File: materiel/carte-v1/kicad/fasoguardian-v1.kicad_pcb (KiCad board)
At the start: 4 copper layers, 41 x 36 mm, 155 parts, among them J3 Antenne LTE, J4 Antenne GNSS active, J5 Nano-SIM, J6 ECT 818011998, J7 SWD Tag-Connect, Q1 2N7002DW, Q2 AO3401A, Q3 2N7002DW, Q4 2N7002DW, Q5 AO3400A, SW1 SOS, U1 STM32U575CIT6, U10 SN74AXC4T774, U11 SN74AXC4T774, U12 ESDA6V1W5, U2 A7670E (variante GNSS), U3 LIS2DW12TR, U4 BQ25180YBGR, U5 TPS63900DSKR, U6 TPS22965DSGR, U7 MAX17048G+T10, U8 ATECC608B-MAHDA, U9 W25Q64JVZPIQ, Y1 32,768 kHz

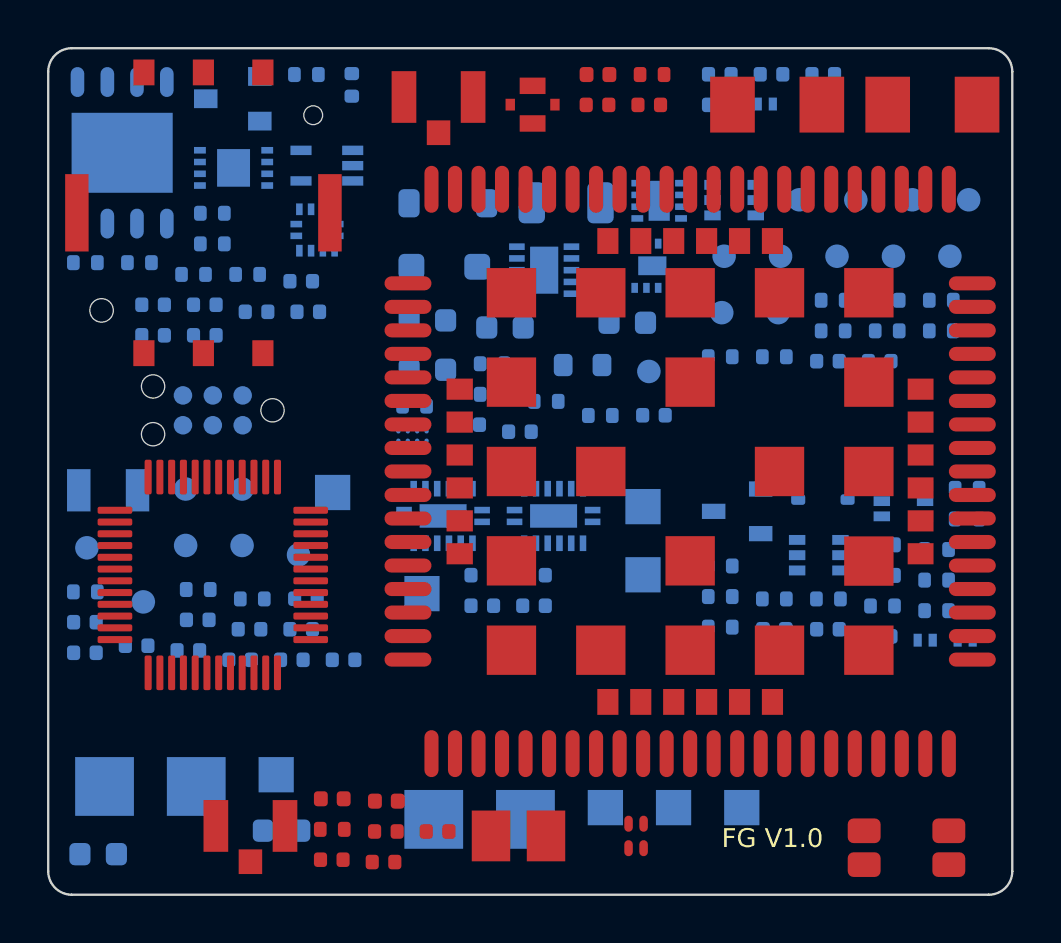
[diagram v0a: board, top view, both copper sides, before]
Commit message: feat(materiel): lignes RF tracées, plans d'alimentation reliés avant routage, routage automatique à 88 %
- lignes LTE et GNSS droites, sans via, de 12,6 et 11,1 mm, réseau d'adaptation aligné, vias de couture
- couche 3 en trois plans (modem, VSYS, 3,3 V), vias de plan posés et verrouillés avant le routage
- Freerouting 2.5 avec éventail ; aucune erreur DRC, parité schéma-carte exacte, 48 liaisons restantes
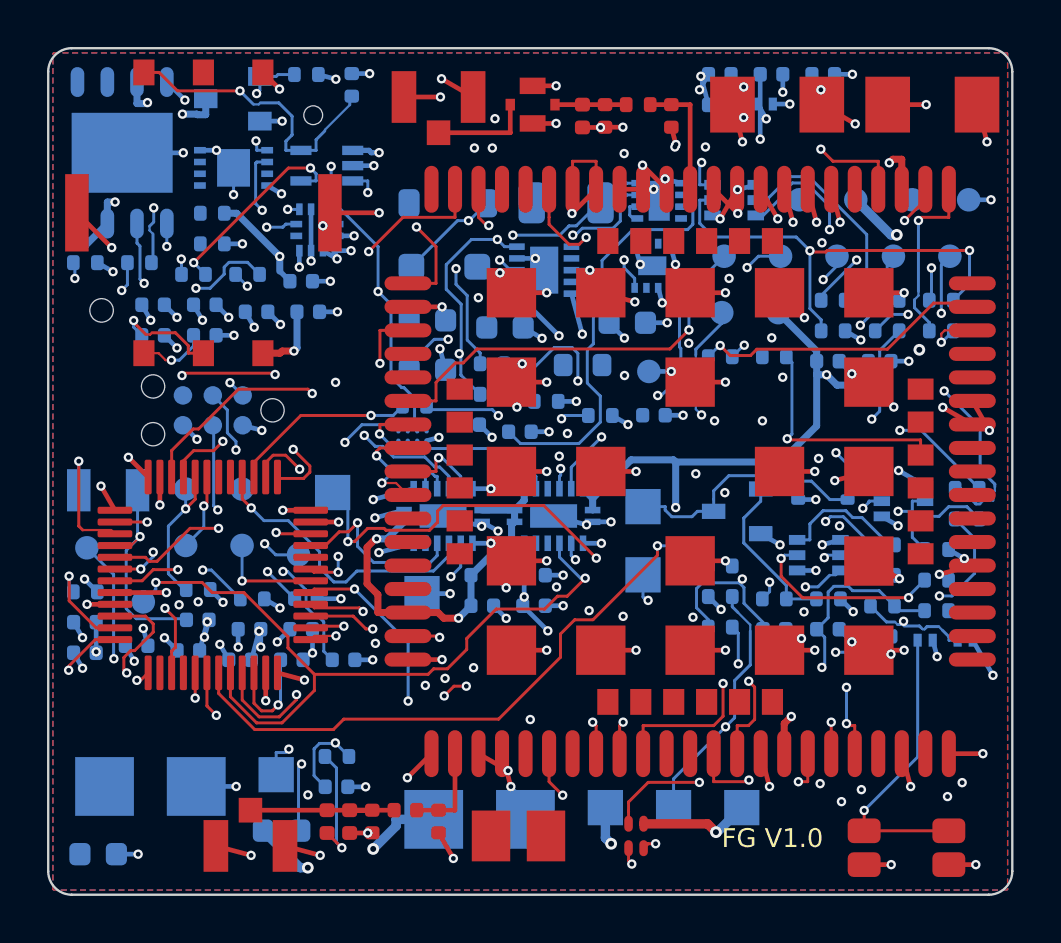
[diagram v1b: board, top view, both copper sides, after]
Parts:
- C25, R23: moved to B.Cu
- moved C25 3.77 mm to (112.3, 131.4)
- moved R23 3.11 mm to (112.3, 130.1)
- moved L2 2.67 mm to (111.9, 132.9), turned to -90 degrees
- moved C23 2.37 mm to (113.8, 132.9), turned to -90 degrees
- moved C22 2.28 mm to (116.6, 132.9), turned to -90 degrees
- moved D4 1.88 mm to (122.7, 102.9), turned to -90 degrees
- moved C24 1.64 mm to (115.2, 132.4), turned to 180 degrees
- moved R20 1.41 mm to (125.1, 102.4), turned to 180 degrees
- moved D5 1.22 mm to (112.8, 132.9), turned to -90 degrees
- moved C20 1.05 mm to (126.5, 102.9), turned to -90 degrees
- moved J4 0.67 mm to (108.6, 133.2), turned to 180 degrees
- moved C21 0.57 mm to (123.7, 102.9), turned to -90 degrees
- turned J6 to 180 degrees
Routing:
- net GND: track 0.00 -> 169.8 mm, vias 0 -> 150
- net I2C_SDA: track 0.00 -> 68.3 mm, vias 0 -> 7
- net 1V8: track 0.00 -> 65.0 mm, vias 0 -> 5
- net SIM_VDD: track 0.00 -> 55.2 mm, vias 0 -> 4
- net SIM_CLK_M: track 0.00 -> 53.2 mm, vias 0 -> 3
- net MCU_PWRKEY: track 0.00 -> 49.5 mm, vias 0 -> 2
- net SIM_RST_M: track 0.00 -> 49.1 mm, vias 0 -> 6
- net LED_R: track 0.00 -> 47.4 mm, vias 0 -> 3
- net GAUGE_ALRT: track 0.00 -> 46.7 mm, vias 0 -> 4
- net MCU_RESET: track 0.00 -> 45.4 mm, vias 0 -> 5
- net MODEM_EN: track 0.00 -> 44.8 mm, vias 0 -> 5
- net SIM_DATA_M: track 0.00 -> 44.2 mm, vias 0 -> 4
- net LOOP: track 0.00 -> 43.4 mm, vias 0 -> 4
- net SOS: track 0.00 -> 41.6 mm, vias 0 -> 3
- net LED_B: track 0.00 -> 40.6 mm, vias 0 -> 3
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- added copper zone on B.Cu, net GND
- added copper zone on F.Cu, net GND
- added copper zone on In2.Cu, net VSYS

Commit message: feat(materiel): carte V1 routée en 6 couches, prête à commander
Routage complet du bracelet sur 41 × 36 mm en 6 couches : aucune liaison
manquante, DRC sans erreur ni avertissement, parité avec le schéma, ERC sans
violation.

- Masse de la couche 2 pleine et interdite aux pistes (référence des lignes
  RF de 50 Ω et de l'USB du modem) ; couche 5 mixte, plans du modem et de la
  batterie interdits aux pistes (ADR 0042, point 9).
- Vias de 0,3/0,15 mm et vias de plan dans les pastilles, bouchés et
  recouverts (capacités JLCPCB en 6 couches).
- Chemin des pointes de 2 A du modem pré-routé et verrouillé, bande de plan
  VBAT dédiée : 25 mΩ de cuivre de la batterie au module au lieu de 140 mΩ
  (ADR 0042, point 10). controler_carte.py le mesure avec resistance.py
  (pistes, vias et plans maillés).
- finir.py : finition par recherche A*, arrachage, négociation de
  congestion, recousage des plans en îlots, permutation et re-routage par
  fenêtre, avec les isolements des classes lus sur la carte ; elargir.py
  ramène les pistes d'alimentation à la largeur de leur classe.
- Dossier de fabrication : Gerber, perçages, netlist, nomenclature et
  placement JLCPCB, plans de montage, rendus, options de commande
  (COMMANDE.md).
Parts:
- L1: moved to B.Cu
- moved C1 29.7 mm to (120.8, 111.2)
- moved D15 26.9 mm to (125.2, 132.2)
- moved D1 26.6 mm to (130.3, 132.2)
- moved F1 26.5 mm to (120.7, 109.1)
- moved L1 25.2 mm to (114.0, 109.0), turned to -90 degrees
- moved R7 23.0 mm to (138.6, 115.3)
- moved C62 20.6 mm to (120.6, 128.1)
- moved U8 20.0 mm to (116.5, 123.2)
- moved C61 20.0 mm to (118.1, 127.3)
- moved C60 19.5 mm to (115.6, 126.9)
- moved U3 18.5 mm to (125.7, 119.5)
- moved TP32 13.2 mm to (132.8, 119.5)
- moved D13 11.1 mm to (128.3, 128.1)
- moved TP31 10.9 mm to (137.5, 132.3)
- moved TP30 10.7 mm to (134.4, 132.3)
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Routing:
- net GND: track 169.8 -> 52.5 mm, vias 150 -> 154
- net BAT_NTC: track 1.54 -> 69.7 mm, vias 1 -> 4
- net VBAT: track 0.00 -> 67.5 mm, vias 0 -> 15
- net I2C_SCL: track 4.23 -> 61.8 mm, vias 2 -> 6
- net VSYS: track 26.2 -> 76.4 mm, vias 9 -> 15
- net FLASH_CS: track 0.00 -> 40.2 mm, vias 0 -> 4
- net 3V3: track 28.1 -> 65.3 mm, vias 28 -> 34
- net SPI_MISO: track 0.00 -> 29.7 mm, vias 0 -> 2
- net VIN: track 0.00 -> 29.5 mm, vias 0 -> 4
- net VIN_EXT: track 9.98 -> 38.3 mm
- net NTC_MES: track 38.5 -> 65.5 mm
- net NTC_EN: track 7.94 -> 32.3 mm, vias 1 -> 3
- net MCU_PWRKEY: track 49.5 -> 31.4 mm
- net MOD_MKIN3: track 37.3 -> 20.6 mm, vias 3 -> 2
- net RI_3V3: track 0.00 -> 16.6 mm, vias 0 -> 2
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- added copper zone on In4.Cu, net 3V3
- added copper zone on In4.Cu, net VBAT
- added copper zone on In4.Cu, net VBAT_MODEM
- added copper zone on In4.Cu, net VSYS
- removed copper zone on In2.Cu, net 3V3
- removed copper zone on In2.Cu, net VBAT_MODEM
- removed copper zone on In2.Cu, net VSYS
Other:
- copper layers 4 -> 6
- board text added: "M+"
- board text added: "M-"
- board text removed: "VB+"
- board text removed: "VB-"

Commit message: fix(materiel): revue complète de la carte V1 avant commande
- microcontrôleur STM32U585CIT6 à la place du STM32U575CIT6, en rupture chez JLCPCB (même brochage, ADR 0042 point 11)
- VBIAS de U6 prise sur la batterie et couloir réservé à la commande du modem : la broche ON n'était plus routable sous le bord du module
- cuivre interne de 1 oz (empilement JLC061211-3313) : chemin du modem à 20 mΩ au lieu de 33 mΩ ; lignes d'antenne à 0,186 mm pour rester à 50 Ω
- placement à la convention JLCPCB (face inférieure à 180° moins l'angle KiCad), empreintes comparées à LCSC, nomenclature par référence LCSC
- hauteurs de la face inférieure d'après les fiches des fabricants (1,35 mm), modèles 3D relatifs au projet, L1 ramenée à 1,2 mm
- finition : vias thermiques en double et cuivre mort retirés ; vias de plan : perçages du même réseau, îlots, via dans la pastille en dégageant le routage
- fiche de commande complète, guide PDF de commande et de mise en service, cahier § 6 tranché
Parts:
- C3: value 1 µF -> 4,7 µF
- U1: value STM32U575CIT6 -> STM32U585CIT6
- moved C65 35.8 mm to (102.8, 125.3), turned to -90 degrees
- moved TP44 25.2 mm to (118.8, 101.6)
- moved TP43 24.8 mm to (116.2, 101.6)
- moved TP45 24.2 mm to (121.4, 101.6)
- moved C64 22.0 mm to (111.6, 125.2)
- moved TP42 20.5 mm to (113.6, 101.6)
- moved C17 19.1 mm to (115.8, 124.0)
- moved R17 15.9 mm to (129.0, 101.1)
- moved R7 15.9 mm to (131.5, 101.1)
- moved R15 15.9 mm to (124.0, 101.1)
- moved R16 15.9 mm to (126.5, 101.1)
- moved RT1 15.3 mm to (134.0, 101.1)
- moved TP33 13.3 mm to (139.0, 123.0)
- moved C70 13.1 mm to (114.1, 119.7), turned to 90 degrees
- moved C16 12.3 mm to (136.8, 106.0)
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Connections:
- U6 pad 4: VBAT_MES -> VBAT
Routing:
- net MCU_RX: track 37.4 -> 116.5 mm, vias 4 -> 14
- net ACC_INT1: track 17.8 -> 79.9 mm, vias 2 -> 3
- net STATUS_3V3: track 17.7 -> 64.5 mm, vias 3 -> 11
- net BAT_NTC: track 69.7 -> 36.7 mm
- net MCU_DTR: track 19.2 -> 49.9 mm, vias 3 -> 6
- net RI_3V3: track 16.6 -> 42.4 mm, vias 2 -> 4
- net MODEM_EN: track 35.7 -> 60.0 mm, vias 2 -> 8
- net TSC_CS: track 23.7 -> 2.07 mm, vias 2 -> 1
- net MCU_TX: track 10.2 -> 29.5 mm, vias 1 -> 2
- net NTC_MES: track 65.5 -> 46.5 mm, vias 4 -> 3
- net CHG_INT: track 32.0 -> 50.3 mm, vias 5 -> 6
- net MCU_RTS: track 5.57 -> 22.6 mm, vias 2 -> 5
- net GNSS_VBKP: track 4.19 -> 21.0 mm
- net VBAT_MES: track 22.9 -> 8.19 mm, vias 5 -> 0
- net VIN_EXT: track 38.3 -> 24.4 mm
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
